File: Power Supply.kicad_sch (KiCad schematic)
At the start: 0 parts

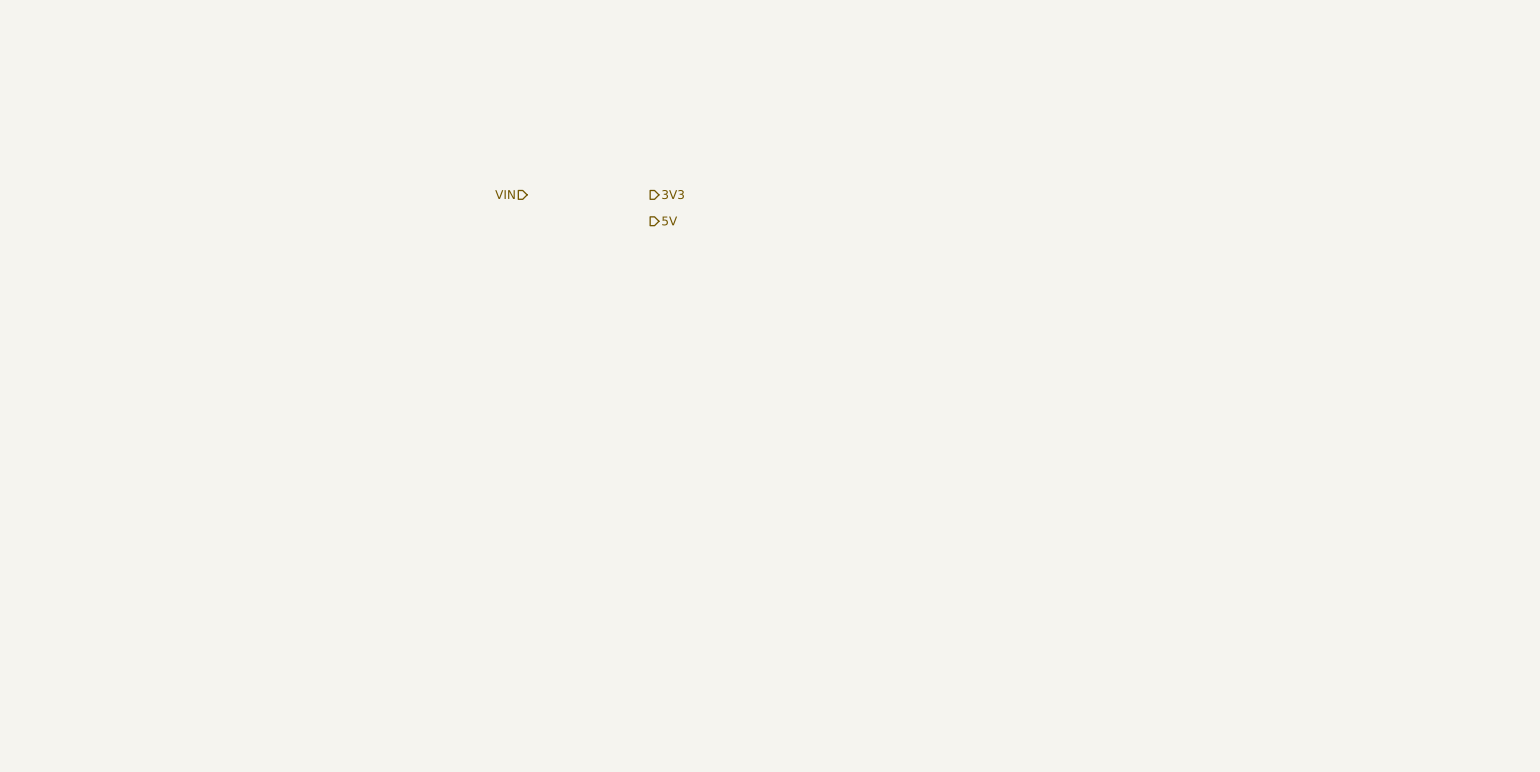
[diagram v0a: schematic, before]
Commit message: power supply circuit schematic done
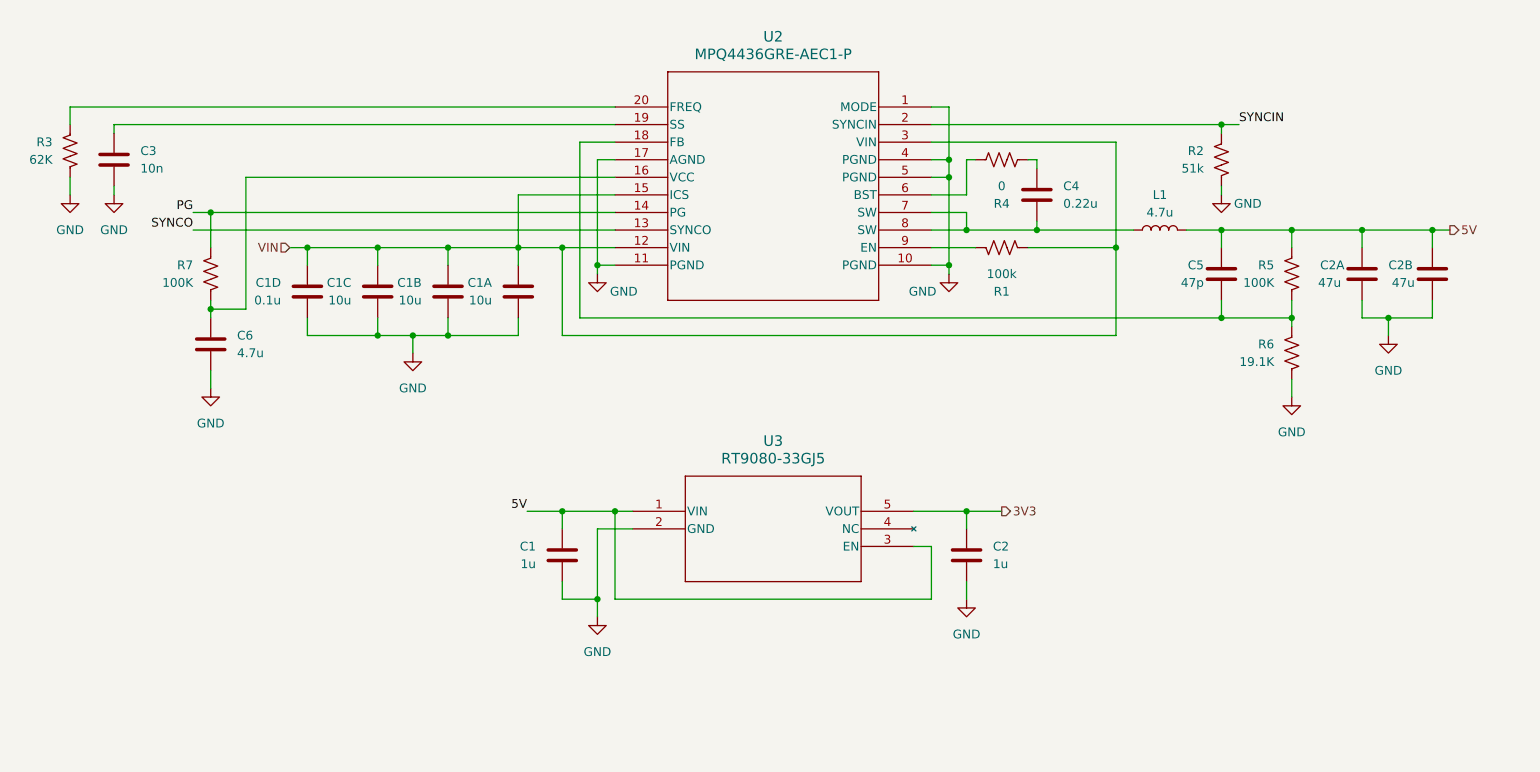
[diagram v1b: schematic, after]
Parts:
- added C1, C2: 1u, symbol Device:C
- added C1A, C1B, C1C: 10u, symbol Device:C
- added C1D: 0.1u, symbol Device:C
- added C2A, C2B: 47u, symbol Device:C
- added C3: 10n, symbol Device:C
- added C4: 0.22u, symbol Device:C
- added C5: 47p, symbol Device:C
- added C6: 4.7u, symbol Device:C
- added L1: 4.7u, symbol Device:L
- added R1: 100k, symbol Device:R_US
- added R2: 51k, symbol Device:R_US
- added R3: 62K, symbol Device:R_US
- added R4: 0, symbol Device:R_US
- added R5, R7: 100K, symbol Device:R_US
- added R6: 19.1K, symbol Device:R_US
- added U2: MPQ4436GRE-AEC1-P, QFN-4x4_MPQ4436-AEC1_MNP, symbol MPQ4436GRE-AEC1-Z:MPQ4436GRE-AEC1-P
- added U3: RT9080-33GJ5, TSOT-23-5_RIT, symbol RT9080_33GJ5:RT9080-33GJ5
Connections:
- net 3V3: now also C2.1, U3.5 (VOUT)
- net 5V: now also C1.1, C2A.1, C2B.1, C5.1, L1.2, R5.1, U3.1 (VIN), U3.3 (EN)
- net VIN: now also C1A.1, C1B.1, C1C.1, C1D.1, R1.2, U2.12 (VIN), U2.15 (ICS), U2.3 (VIN)
- new net: C4.1, L1.1, U2.7 (SW), U2.8 (SW)
- new net: C3.1, U2.19 (SS)
- new net: C5.2, R5.2, R6.1, U2.18 (FB)
- new net: C4.2, R4.1
- new net: R4.2, U2.6 (BST)
- new net: C6.1, R7.2, U2.16 (VCC)
- new net: R3.1, U2.20 (FREQ)
- new net: R1.1, U2.9 (EN)
- new net GND: C1.2, C1A.2, C1B.2, C1C.2, C1D.2, C2.2, C2A.2, C2B.2, C3.2, C6.2, R2.1, R3.2, R6.2, U2.1 (MODE), U2.10 (PGND), U2.11 (PGND), U2.17 (AGND), U2.4 (PGND), U2.5 (PGND), U3.2 (GND)
- new net PG: R7.1, U2.14 (PG)
- new net SYNCIN: R2.2, U2.2 (SYNCIN)
- new net SYNCO: U2.13 (SYNCO)

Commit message: working on ignition and power output sheets
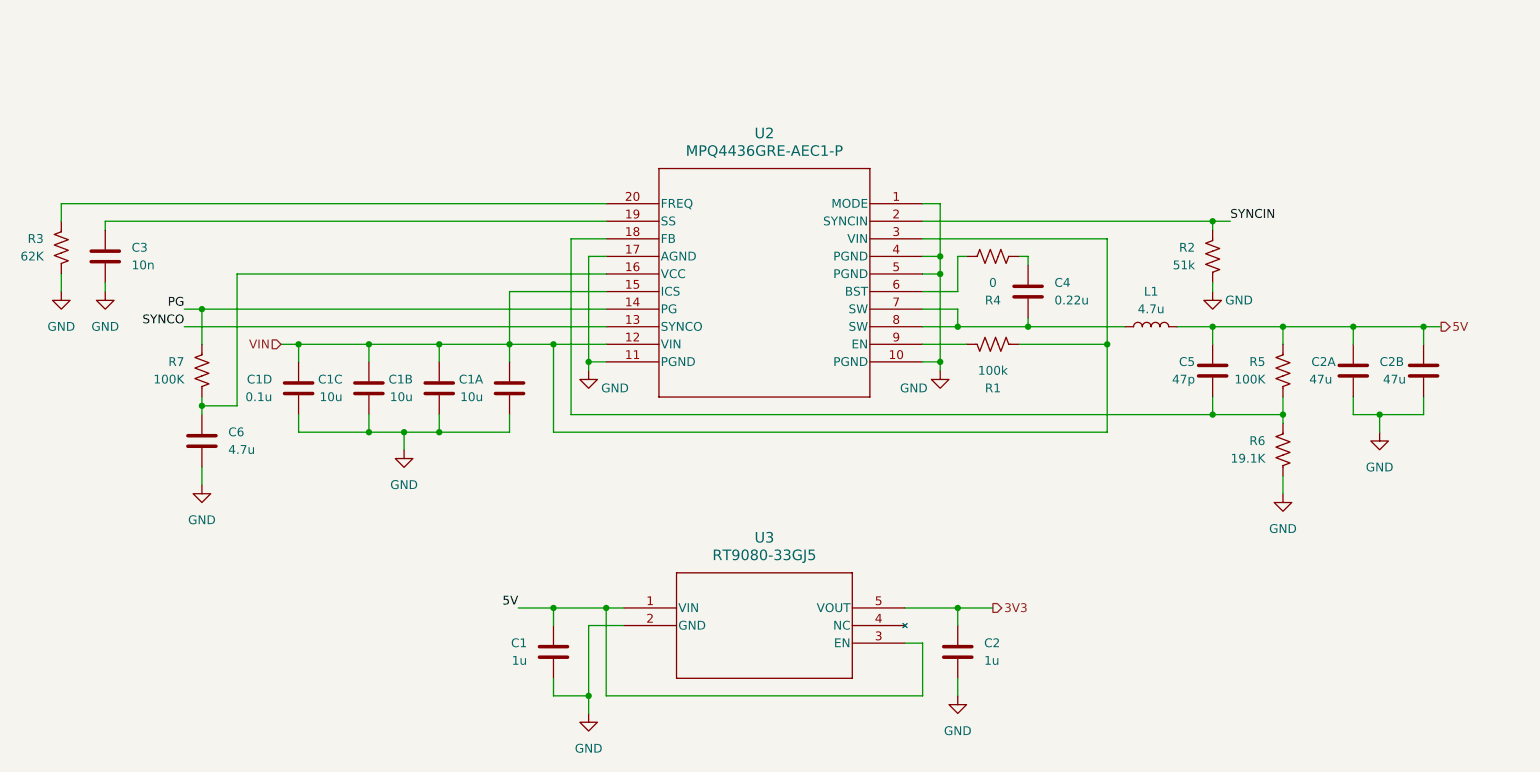
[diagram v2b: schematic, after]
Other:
- moved on the sheet: C1, C1A, C1B, C1C, C1D, C2, C2A, C2B, C3, C4, C5, C6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

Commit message: switch Ignition page to use load drivers rather than discrete FETs
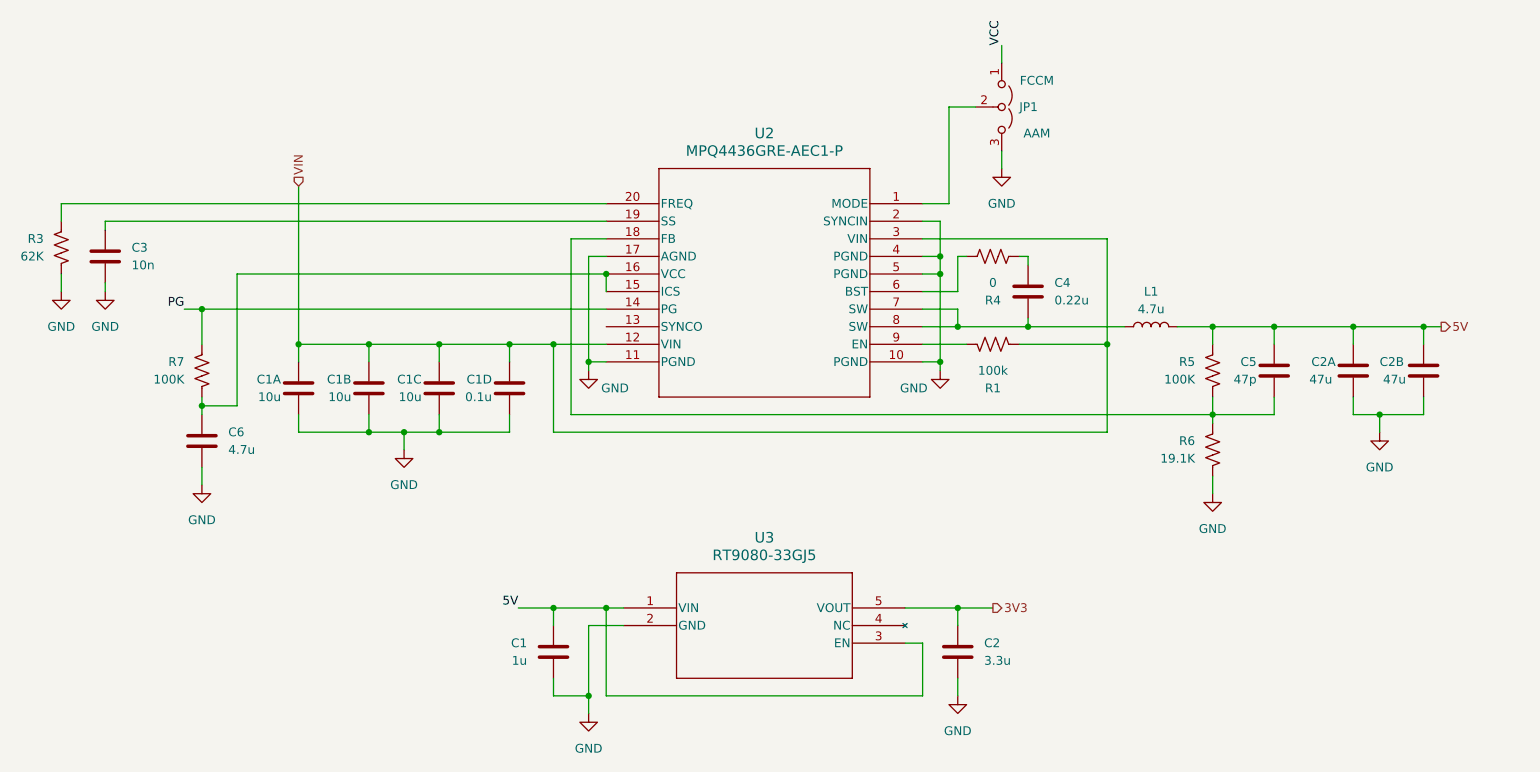
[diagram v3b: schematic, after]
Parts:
- removed R2: 51k, symbol Device:R_US
- added JP1: ~, symbol Jumper:Jumper_3_Open
- C2: value 1u -> 3.3u
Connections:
- net SYNCIN is gone; now on net GND: U2.2 (SYNCIN)
- net GND: now also JP1.3 (B); no longer U2.1 (MODE)
- net VIN: no longer U2.15 (ICS)
- net at C6.1, R7.2, U2.16 (VCC): now also U2.15 (ICS)
- net SYNCO: no longer names the net of U2.13 (SYNCO)
- new net: JP1.2 (C), U2.1 (MODE)
- new net VCC: JP1.1 (A)
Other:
- company: (none) -> J2B
- moved on the sheet: C1A, C1B, C1C, C1D, C5, R5, R6

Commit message: fix ERC errors
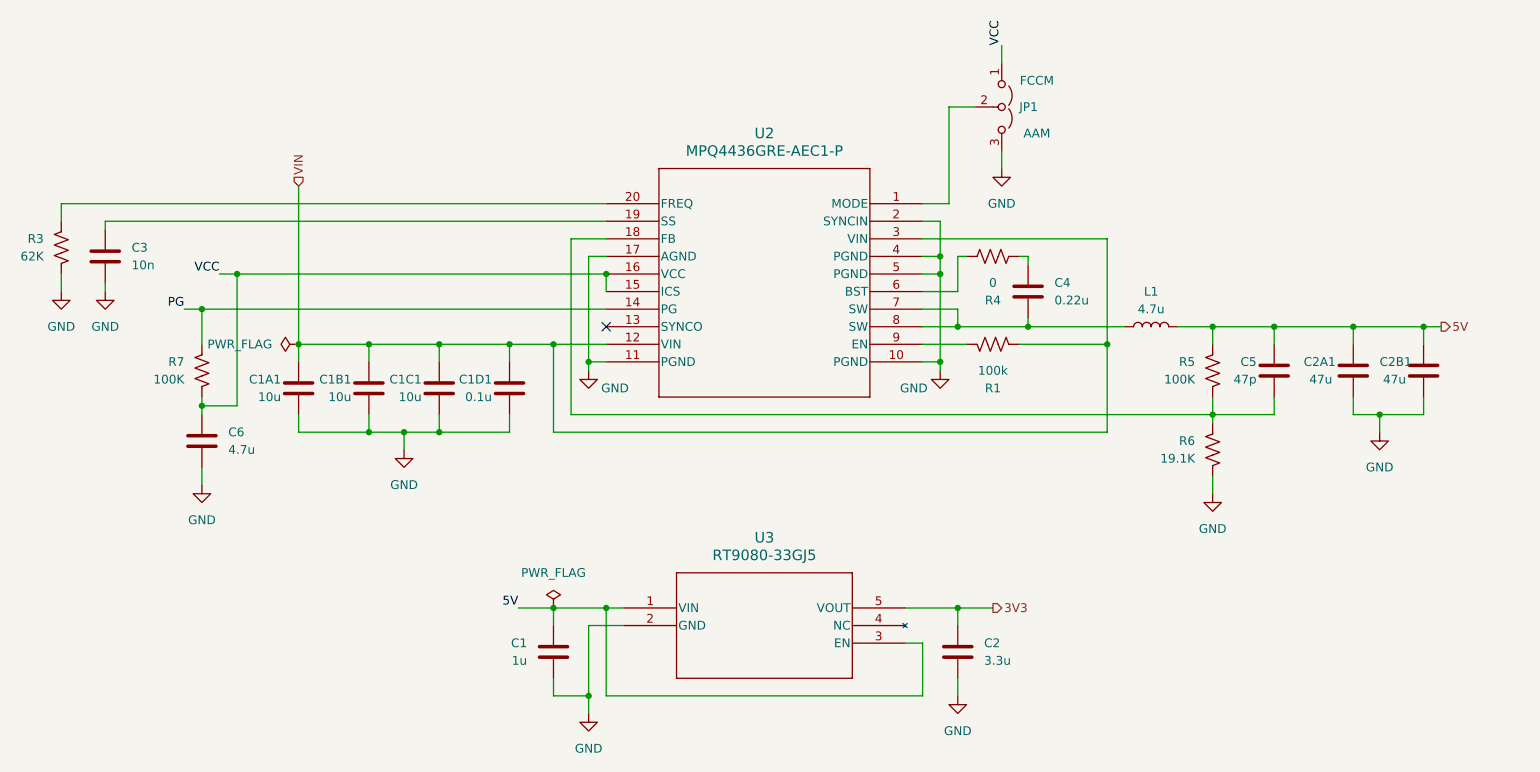
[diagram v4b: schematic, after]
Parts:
- renumbered C1A to C1A1, C1B to C1B1, C1C to C1C1, C1D to C1D1, C2A to C2A1, C2B to C2B1
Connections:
- net VCC: now also C6.1, R7.2, U2.15 (ICS), U2.16 (VCC)
- no-connect marks 0 -> 1
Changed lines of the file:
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@@
   (junction (at 222.25 82.55) (diameter 0) (color 0 0 0 0)
   )
+  (junction (at 72.39 74.93) (diameter 0) (color 0 0 0 0)
+  )
   (junction (at 233.68 82.55) (diameter 0) (color 0 0 0 0)
   )
@@
   (junction (at 213.36 82.55) (diameter 0) (color 0 0 0 0)
   )
+  (no_connect (at 125.73 82.55))
   (wire (pts (xy 125.73 69.85) (xy 120.65 69.85))
     (stroke (width 0) (type default))
@@
   )
   (wire (pts (xy 213.36 92.71) (xy 213.36 95.25))
+    (stroke (width 0) (type default))
+  )
+  (wire (pts (xy 69.85 74.93) (xy 72.39 74.93))
     (stroke (width 0) (type default))
   )
@@
   )
   (label "PG" (at 64.77 80.01 180) (fields_autoplaced)
+    (effects (font (size 1.27 1.27)) (justify right bottom))
+  )
+  (label "VCC" (at 69.85 74.93 180) (fields_autoplaced)
     (effects (font (size 1.27 1.27)) (justify right bottom))
   )
@@
   (symbol (lib_id "Device:C") (at 233.68 88.9 0) (mirror y) (unit 1)
     (in_bom yes) (on_board yes) (dnp no)
-    (property "Reference" "C2B" (at 237.49 87.63 0)
+    (property "Reference" "C2B1" (at 237.49 87.63 0)
       (effects (font (size 1.27 1.27)) (justify right))
     )
@@
       (project "control-module-pcb"
         (path "/4c946e98-79c2-4a2d-bd7f-2a33db8d8c91/a3db59ba-0e1f-4e6c-a45d-0dd013b5118e"
-          (reference "C2B") (unit 1)
+          (reference "C2B1") (unit 1)
         )
       )
@@
   (symbol (lib_id "Device:C") (at 111.76 91.44 0) (mirror y) (unit 1)
     (in_bom yes) (on_board yes) (dnp no)
-    (property "Reference" "C1D" (at 109.22 90.17 0)
+    (property "Reference" "C1D1" (at 109.22 90.17 0)
       (effects (font (size 1.27 1.27)) (justify left))
     )
@@
       (project "control-module-pcb"
         (path "/4c946e98-79c2-4a2d-bd7f-2a33db8d8c91/a3db59ba-0e1f-4e6c-a45d-0dd013b5118e"
-          (reference "C1D") (unit 1)
+          (reference "C1D1") (unit 1)
         )
       )
@@
   (symbol (lib_id "Device:C") (at 81.28 91.44 0) (mirror y) (unit 1)
     (in_bom yes) (on_board yes) (dnp no)
-    (property "Reference" "C1A" (at 78.74 90.17 0)
+    (property "Reference" "C1A1" (at 78.74 90.17 0)
       (effects (font (size 1.27 1.27)) (justify left))
     )
@@
       (project "control-module-pcb"
         (path "/4c946e98-79c2-4a2d-bd7f-2a33db8d8c91/a3db59ba-0e1f-4e6c-a45d-0dd013b5118e"
-          (reference "C1A") (unit 1)
+          (reference "C1A1") (unit 1)
+        )
+      )
+    )
+  )
+  (symbol (lib_id "power:PWR_FLAG") (at 118.11 123.19 0) (unit 1)
+    (in_bom yes) (on_board yes) (dnp no) (fields_autoplaced)
+    (property "Reference" "#FLG01" (at 118.11 121.285 0)
+      (effects (font (size 1.27 1.27)) hide)
+    )
+    (property "Value" "PWR_FLAG" (at 118.11 118.11 0)
+      (effects (font (size 1.27 1.27)))
+    )
+    (property "Footprint" "" (at 118.11 123.19 0)
+      (effects (font (size 1.27 1.27)) hide)
+    )
+    (property "Datasheet" "~" (at 118.11 123.19 0)
+      (effects (font (size 1.27 1.27)) hide)
+    )
+    (pin "1")
+    (instances
+      (project "control-module-pcb"
+        (path "/4c946e98-79c2-4a2d-bd7f-2a33db8d8c91/a3db59ba-0e1f-4e6c-a45d-0dd013b5118e"
+          (reference "#FLG01") (unit 1)
         )
       )
@@
       (effects (font (size 1.27 1.27) italic) hide)
     )
-    (pin "1")
-    (pin "10")
-    (pin "11")
     (pin "12")
     (pin "13")
     (pin "14")
+    (pin "18")
+    (pin "19")
+    (pin "2")
+    (pin "3")
+    (pin "7")
+    (pin "1")
+    (pin "10")
+    (pin "11")
     (pin "15")
     (pin "16")
     (pin "17")
-    (pin "18")
-    (pin "19")
-    (pin "2")
     (pin "20")
-    (pin "3")
     (pin "4")
     (pin "5")
     (pin "6")
-    (pin "7")
     (pin "8")
     (pin "9")
@@
   (symbol (lib_id "Device:C") (at 101.6 91.44 0) (mirror y) (unit 1)
     (in_bom yes) (on_board yes) (dnp no)
-    (property "Reference" "C1C" (at 99.06 90.17 0)
+    (property "Reference" "C1C1" (at 99.06 90.17 0)
       (effects (font (size 1.27 1.27)) (justify left))
     )
@@
       (project "control-module-pcb"
         (path "/4c946e98-79c2-4a2d-bd7f-2a33db8d8c91/a3db59ba-0e1f-4e6c-a45d-0dd013b5118e"
-          (reference "C1C") (unit 1)
+          (reference "C1C1") (unit 1)
         )
       )
@@
   (symbol (lib_id "Device:C") (at 243.84 88.9 0) (mirror y) (unit 1)
     (in_bom yes) (on_board yes) (dnp no)
-    (property "Reference" "C2A" (at 231.14 87.63 0)
+    (property "Reference" "C2A1" (at 231.14 87.63 0)
       (effects (font (size 1.27 1.27)) (justify left))
     )
@@
       (project "control-module-pcb"
         (path "/4c946e98-79c2-4a2d-bd7f-2a33db8d8c91/a3db59ba-0e1f-4e6c-a45d-0dd013b5118e"
-          (reference "C2A") (unit 1)
+          (reference "C2A1") (unit 1)
         )
       )
@@
         (path "/4c946e98-79c2-4a2d-bd7f-2a33db8d8c91/a3db59ba-0e1f-4e6c-a45d-0dd013b5118e"
           (reference "#PWR09") (unit 1)
+        )
+      )
+    )
+  )
+  (symbol (lib_id "power:PWR_FLAG") (at 81.28 85.09 90) (unit 1)
+    (in_bom yes) (on_board yes) (dnp no) (fields_autoplaced)
+    (property "Reference" "#FLG02" (at 79.375 85.09 0)
+      (effects (font (size 1.27 1.27)) hide)
+    )
+    (property "Value" "PWR_FLAG" (at 77.47 85.09 90)
+      (effects (font (size 1.27 1.27)) (justify left))
+    )
+    (property "Footprint" "" (at 81.28 85.09 0)
+      (effects (font (size 1.27 1.27)) hide)
+    )
+    (property "Datasheet" "~" (at 81.28 85.09 0)
+      (effects (font (size 1.27 1.27)) hide)
+    )
+    (pin "1")
+    (instances
+      (project "control-module-pcb"
+        (path "/4c946e98-79c2-4a2d-bd7f-2a33db8d8c91/a3db59ba-0e1f-4e6c-a45d-0dd013b5118e"
+          (reference "#FLG02") (unit 1)
         )
       )
@@
   (symbol (lib_id "Device:C") (at 91.44 91.44 0) (mirror y) (unit 1)
     (in_bom yes) (on_board yes) (dnp no)
-    (property "Reference" "C1B" (at 88.9 90.17 0)
+    (property "Reference" "C1B1" (at 88.9 90.17 0)
       (effects (font (size 1.27 1.27)) (justify left))
     )
@@
       (project "control-module-pcb"
         (path "/4c946e98-79c2-4a2d-bd7f-2a33db8d8c91/a3db59ba-0e1f-4e6c-a45d-0dd013b5118e"
-          (reference "C1B") (unit 1)
-        )
-      )
+          (reference "C1B1") (unit 1)
+        )
+      )
